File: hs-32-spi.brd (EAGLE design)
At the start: 15.2 x 23.5 mm, 19 parts, among them U1 RHD2132_QFN, U2 ADXL335

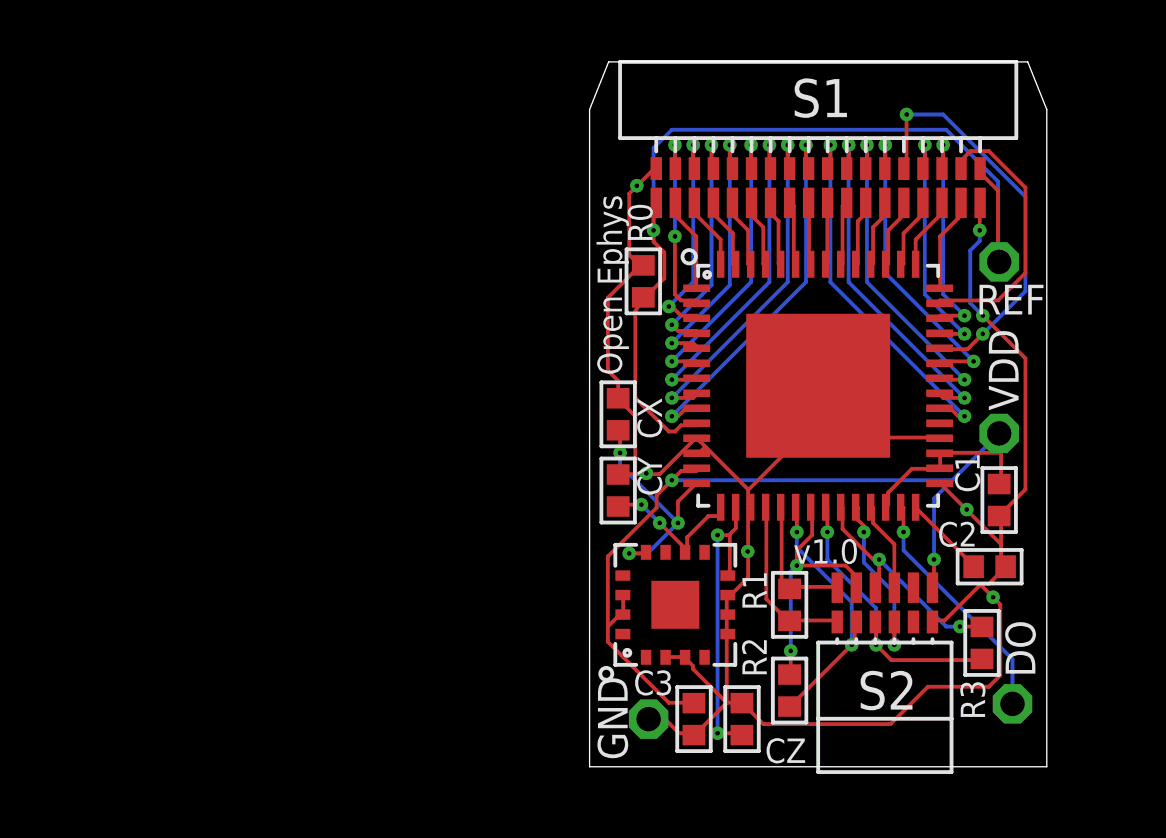
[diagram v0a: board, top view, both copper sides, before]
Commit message: Added initial attempt of adding an expansion connector.
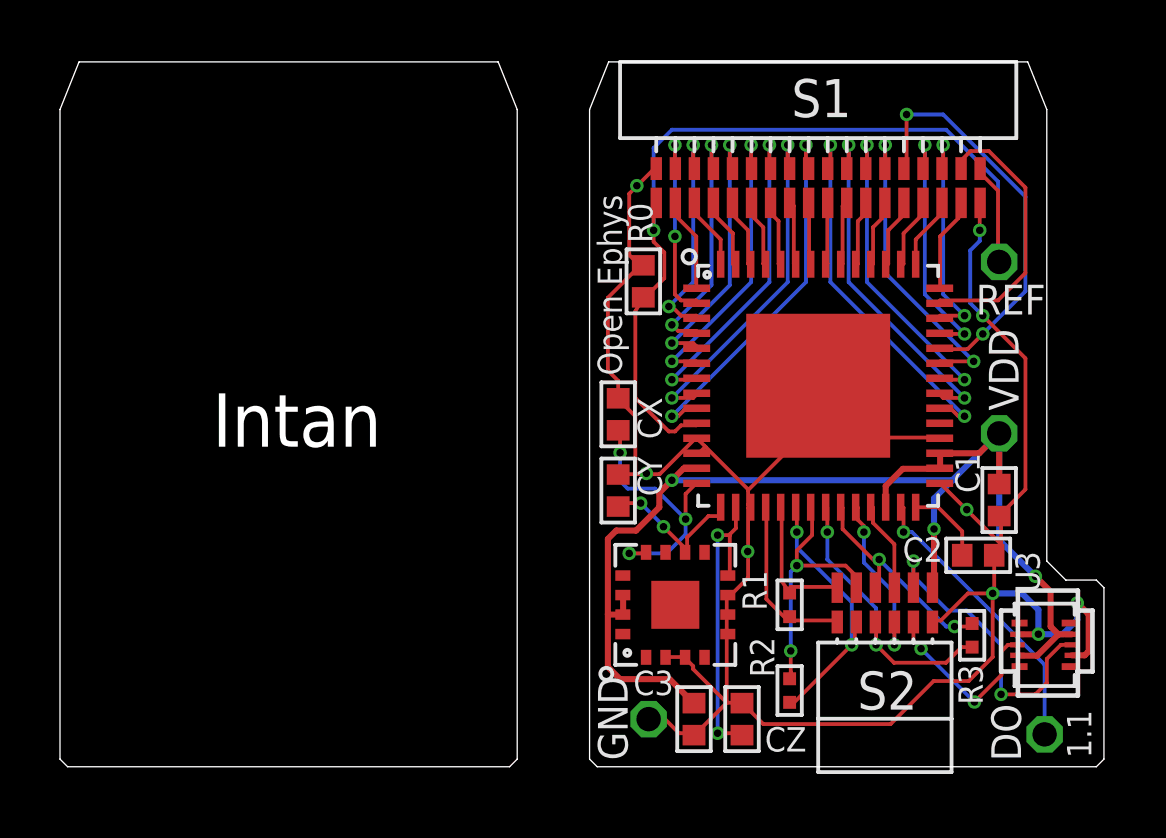
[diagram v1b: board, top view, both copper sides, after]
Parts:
- added U3: (no value), Molex 5050700622:MOLEX_5050700622
- R1, R2, R3: device RHD2000_eval_board:0402 -> RHD2000_eval_board:0201
- moved DO 1.48 mm to (15.2, 1.08)
- moved C2 0.54 mm to (13.0, 7.05)
- moved R3 0.42 mm to (12.8, 4.38)
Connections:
- new net SCL: S2.T5, U3.3
- new net SDA: S2.B5, U3.4
- net GND: now also U3.1, U3.6
- net VCC: now also U3.2, U3.5
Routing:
- net SCL: track 0.00 -> 10.4 mm, vias 0 -> 2
- net VCC: track 35.3 -> 45.3 mm, vias 2 -> 3
- net GND: track 73.6 -> 80.3 mm, vias 7 -> 9
- net SDA: track 0.00 -> 6.19 mm, vias 0 -> 2
- net N$43: track 8.14 -> 9.76 mm
- net XOUT: track 8.13 -> 9.01 mm
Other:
- board size 15.2 x 23.5 mm -> 34.8 x 23.5 mm
- board text added: "1.1"
- board text added: "Intan"
- board text removed: "v1.0"

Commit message: Changed location of Omnetics connector closer to headstage center.
. This allowed space to move the new expansion connector to a position where there's no need to increase the headstage size.

TO DO
. Complete the layout.
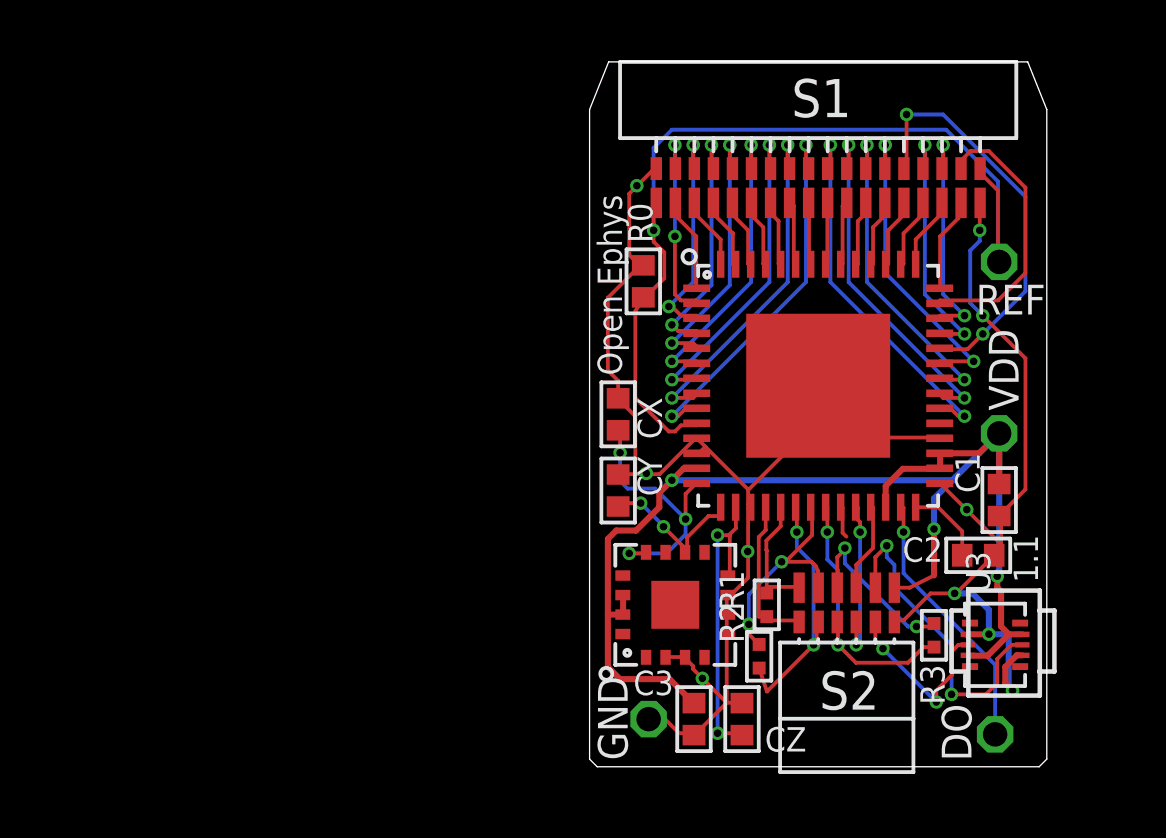
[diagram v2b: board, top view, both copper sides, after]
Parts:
- moved DO 1.65 mm to (13.5, 1.08)
- moved U3 1.65 mm to (13.5, 4.06)
- moved R2 1.53 mm to (5.65, 3.68)
- moved R3 1.27 mm to (11.5, 4.38)
- moved S2 1.27 mm to (8.57, 3.81)
- moved R1 0.76 mm to (5.91, 5.40)
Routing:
- net GND: track 80.3 -> 68.5 mm, vias 9 -> 10
- net N$37: track 8.57 -> 7.63 mm
- net N$43: track 9.76 -> 8.92 mm
- net N$11: track 5.94 -> 5.21 mm
- net N$39: track 7.60 -> 7.02 mm
- net N$38: track 9.73 -> 9.21 mm
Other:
- board size 34.8 x 23.5 mm -> 15.2 x 23.5 mm
- board text removed: "Intan"

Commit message: Finished layout for v1.1
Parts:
- moved CZ 0.32 mm to (4.76, 1.59)
- moved R3 0.13 mm to (11.6, 4.38)
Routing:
- net VCC: track 45.6 -> 19.9 mm, vias 3 -> 4
- net GND: track 68.5 -> 43.1 mm, vias 10 -> 11
- net N$40: track 5.49 -> 6.52 mm
- net N$38: track 9.21 -> 10.2 mm
- net N$36: track 8.69 -> 8.15 mm
